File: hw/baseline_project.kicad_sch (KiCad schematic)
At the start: 20 parts, among them J101 EXT_3V3, Q101 IRLD024PBF, SW101 UP, SW102 DOWN, SW103 LEFT, SW104 RIGHT, SW105 MODE, U101 EK-TM4C123GXL, U102 ESP8266-1, U103 Adafruit ST7735R

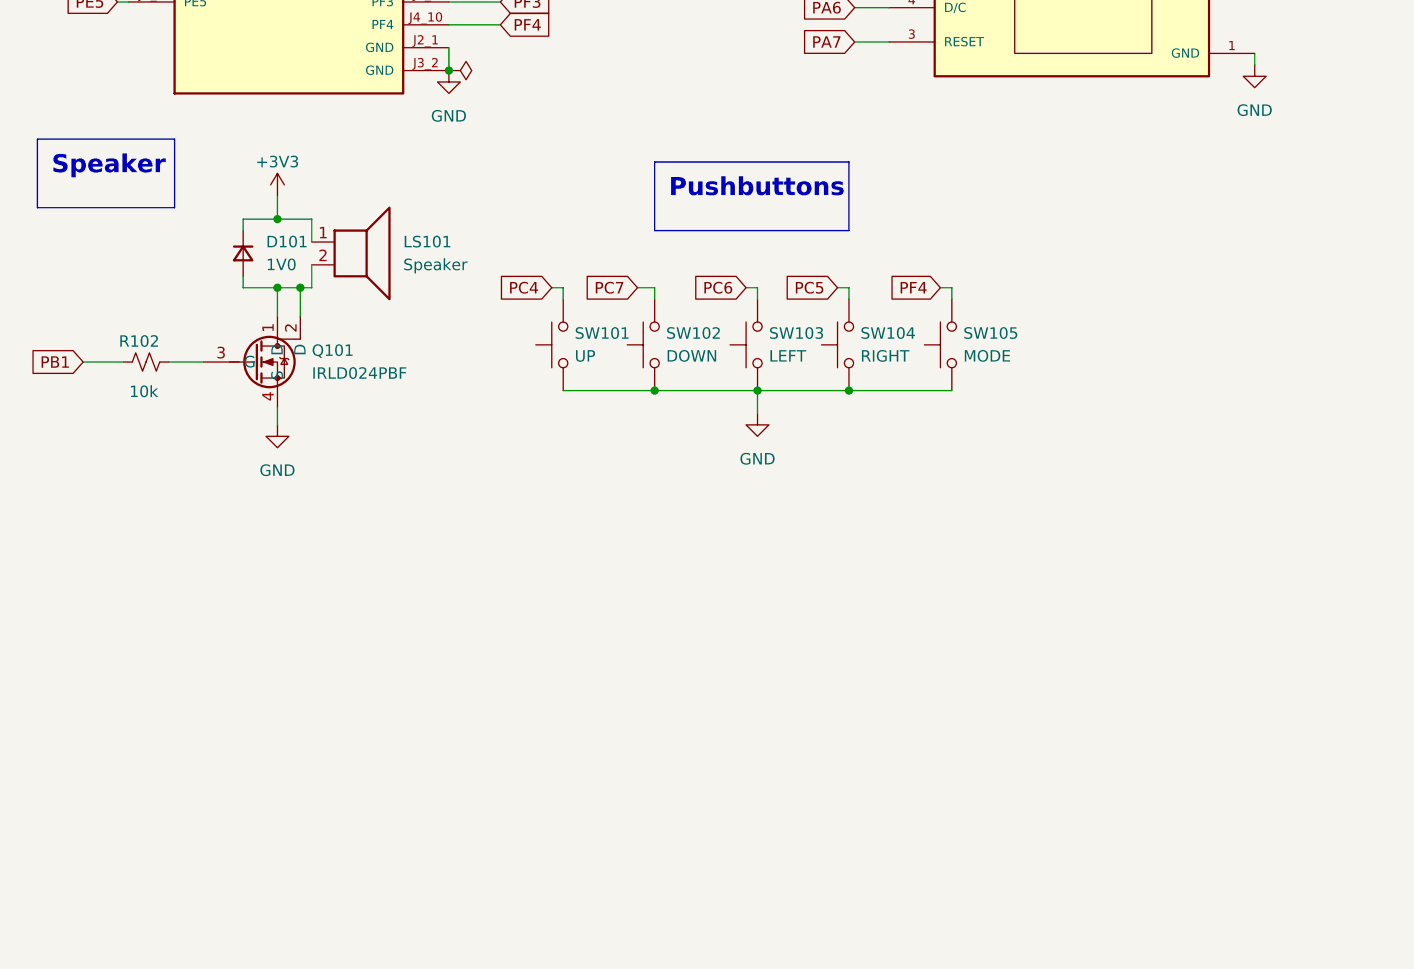
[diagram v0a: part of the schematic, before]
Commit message: Function and module prototypes
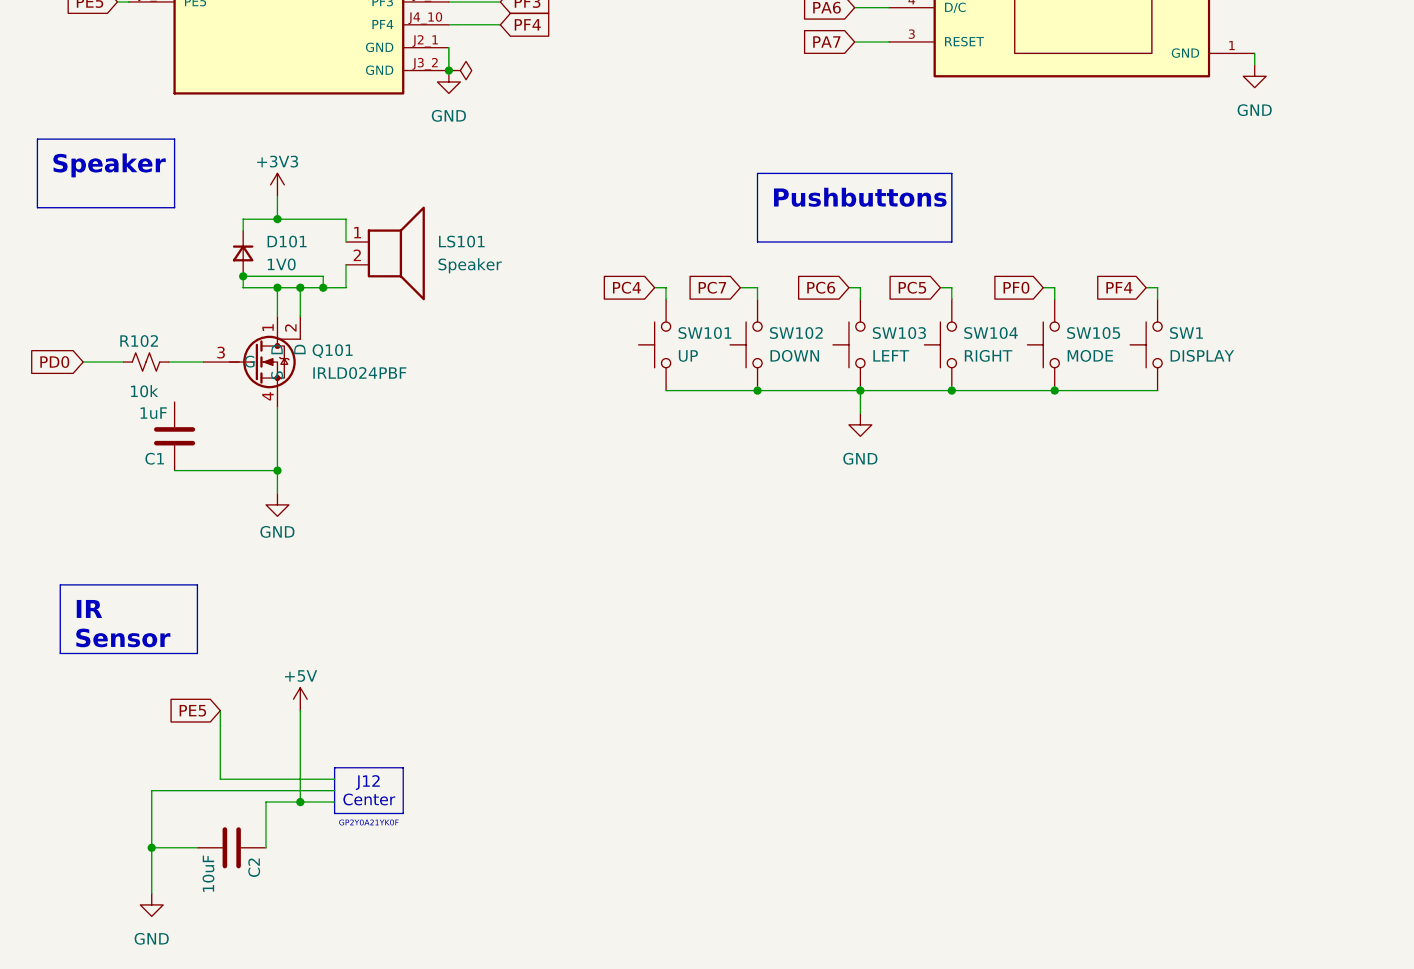
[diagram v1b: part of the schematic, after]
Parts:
- added C1: 1uF, ECE445L:C_Axial_200mil, symbol ECE445L:C
- added C2: 10uF, ECE445L:C_Axial_200mil, symbol ECE445L:C
- added SW1: DISPLAY, Button_Switch_THT:SW_PUSH_6mm, symbol Switch:SW_Push
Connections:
- net +5V: now also C2.1
- net GND: now also C1.1, C2.2, SW1.1
- net PB1: no longer R102.1
- net PD0: now also R102.1
- net PF0: now also SW105.2
- net PF4: now also SW1.2; no longer SW105.2
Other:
- note added: "GP2Y0A21YK0F"
- note added: "J12 Center"
- moved on the sheet: LS101, SW101, SW102, SW103, SW104, SW105
